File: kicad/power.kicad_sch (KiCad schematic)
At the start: 51 parts, among them J4 TYPE-C-31-M-12, Q7 BC847BW,115, U10 MC34063AD, U11 MC34063AD, U12 XC6206P332MR-G, U13 TPS2116DRLR, U9 TPD4S012DRYR

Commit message: [kicad] Fixed inductor footprints | TODO: integrate in actual pcb
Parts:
- L1, L2: footprint Inductor_SMD:L_1210_3225Metric -> bldc:CY105-100uH
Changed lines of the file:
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@@
       (effects (font (size 1.27 1.27)))
     )
-    (property "Footprint" "Inductor_SMD:L_1210_3225Metric" (at 45.72 85.09 0)
+    (property "Footprint" "bldc:CY105-100uH" (at 45.72 85.09 0)
       (effects (font (size 1.27 1.27)) hide)
     )
@@
       (effects (font (size 1.27 1.27)))
     )
-    (property "Footprint" "Inductor_SMD:L_1210_3225Metric" (at 43.18 34.29 0)
-      (effects (font (size 1.27 1.27)) hide)
-    )
+    (property "Footprint" "bldc:CY105-100uH" (at 43.18 34.29 0)
+      (effects (font (size 1.27 1.27)) hide)
+    )

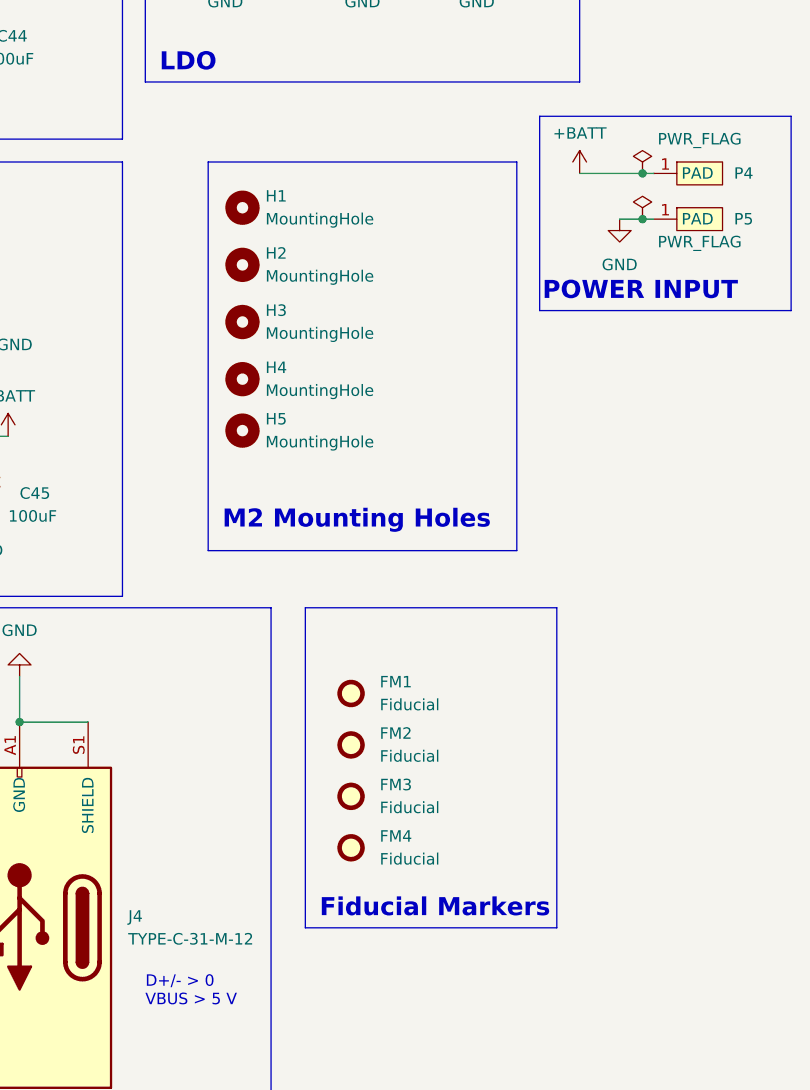
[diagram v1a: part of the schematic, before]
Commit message: changed inductors, rearranged new FET footprints and symbols
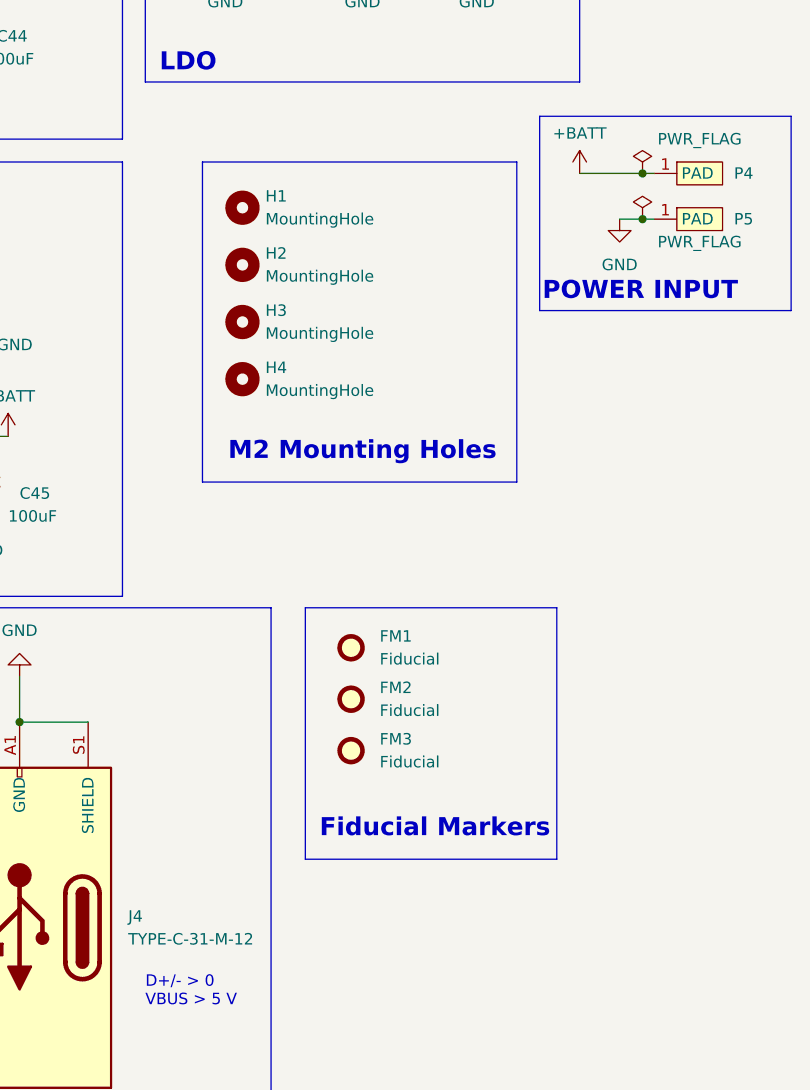
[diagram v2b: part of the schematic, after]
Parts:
- removed FM4: Fiducial, Fiducial:Fiducial_1mm_Mask2mm, symbol Mechanical:Fiducial
- removed H5: MountingHole, bldc:MountingHole_1.152mm_jlcpcb, symbol Mechanical:MountingHole
- L1, L2: footprint bldc:CY105-100uH -> L_Sunlord_SWPA6045S; MFR.Part (none) -> SWPA6045S101MT; jlcpcb (none) -> C60633
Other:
- moved on the sheet: FM1, FM2, FM3
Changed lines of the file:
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@@
     (fill (type none))
   )
-  (rectangle (start 127 114.3) (end 154.94 149.86)
+  (rectangle (start 127 114.3) (end 154.94 142.24)
     (stroke (width 0) (type default))
     (fill (type none))
@@
     (fill (type none))
   )
-  (rectangle (start 116.205 64.77) (end 150.495 107.95)
+  (rectangle (start 115.57 64.77) (end 150.495 100.33)
     (stroke (width 0) (type default))
     (fill (type none))
@@
   )
   (text_box "Fiducial Markers"
-    (at 127 144.78 0) (size 34.29 5.08)
+    (at 127 135.89 0) (size 34.29 5.08)
     (stroke (width -0.0001) (type default))
     (fill (type none))
@@
   )
   (text_box "M2 Mounting Holes"
-    (at 116.205 101.6 0) (size 34.29 5.08)
+    (at 116.84 93.98 0) (size 34.29 5.08)
     (stroke (width -0.0001) (type default))
     (fill (type none))
@@
     )
   )
-  (symbol (lib_id "Mechanical:Fiducial") (at 132.08 123.825 0) (unit 1)
-    (in_bom yes) (on_board yes) (dnp no) (fields_autoplaced)
-    (property "Reference" "FM1" (at 135.255 122.555 0)
-      (effects (font (size 1.27 1.27)) (justify left))
-    )
-    (property "Value" "Fiducial" (at 135.255 125.095 0)
-      (effects (font (size 1.27 1.27)) (justify left))
-    )
-    (property "Footprint" "Fiducial:Fiducial_1mm_Mask2mm" (at 132.08 123.825 0)
-      (effects (font (size 1.27 1.27)) hide)
-    )
-    (property "Datasheet" "~" (at 132.08 123.825 0)
+  (symbol (lib_id "Mechanical:Fiducial") (at 132.08 118.745 0) (unit 1)
+    (in_bom yes) (on_board yes) (dnp no) (fields_autoplaced)
+    (property "Reference" "FM1" (at 135.255 117.475 0)
+      (effects (font (size 1.27 1.27)) (justify left))
+    )
+    (property "Value" "Fiducial" (at 135.255 120.015 0)
+      (effects (font (size 1.27 1.27)) (justify left))
+    )
+    (property "Footprint" "Fiducial:Fiducial_1mm_Mask2mm" (at 132.08 118.745 0)
+      (effects (font (size 1.27 1.27)) hide)
+    )
+    (property "Datasheet" "~" (at 132.08 118.745 0)
       (effects (font (size 1.27 1.27)) hide)
     )
@@
       (effects (font (size 1.27 1.27)))
     )
-    (property "Footprint" "bldc:CY105-100uH" (at 45.72 85.09 0)
-      (effects (font (size 1.27 1.27)) hide)
-    )
-    (property "Datasheet" "https://wmsc.lcsc.com/wmsc/upload/file/pdf/v2/lcsc/2208231730_SHOU-HAN-CY105-100uH_C5140330.pdf" (at 45.72 85.09 0)
+    (property "Footprint" "L_Sunlord_SWPA6045S" (at 45.72 85.09 0)
+      (effects (font (size 1.27 1.27)) hide)
+    )
+    (property "Datasheet" "https://wmsc.lcsc.com/wmsc/upload/file/pdf/v2/lcsc/2310251551_Sunlord-SWPA6045S101MT_C60633.pdf" (at 45.72 85.09 0)
+      (effects (font (size 1.27 1.27)) hide)
+    )
+    (property "MFR.Part" "SWPA6045S101MT" (at 45.72 85.09 0)
+      (effects (font (size 1.27 1.27)) hide)
+    )
+    (property "jlcpcb" "C60633" (at 45.72 85.09 0)
       (effects (font (size 1.27 1.27)) hide)
     )
@@
       (effects (font (size 1.27 1.27)))
     )
-    (property "Footprint" "bldc:CY105-100uH" (at 43.18 34.29 0)
-      (effects (font (size 1.27 1.27)) hide)
-    )
-    (property "Datasheet" "https://wmsc.lcsc.com/wmsc/upload/file/pdf/v2/lcsc/2208231730_SHOU-HAN-CY105-100uH_C5140330.pdf" (at 43.18 34.29 0)
+    (property "Footprint" "L_Sunlord_SWPA6045S" (at 43.18 34.29 0)
+      (effects (font (size 1.27 1.27)) hide)
+    )
+    (property "Datasheet" "https://wmsc.lcsc.com/wmsc/upload/file/pdf/v2/lcsc/2310251551_Sunlord-SWPA6045S101MT_C60633.pdf" (at 43.18 34.29 0)
+      (effects (font (size 1.27 1.27)) hide)
+    )
+    (property "MFR.Part" "SWPA6045S101MT" (at 43.18 34.29 0)
+      (effects (font (size 1.27 1.27)) hide)
+    )
+    (property "jlcpcb" "C60633" (at 43.18 34.29 0)
       (effects (font (size 1.27 1.27)) hide)
     )
@@
     )
   )
-  (symbol (lib_id "Mechanical:MountingHole") (at 120.015 94.615 0) (unit 1)
-    (in_bom yes) (on_board yes) (dnp no) (fields_autoplaced)
-    (property "Reference" "H5" (at 122.555 93.345 0)
-      (effects (font (size 1.27 1.27)) (justify left))
-    )
-    (property "Value" "MountingHole" (at 122.555 95.885 0)
-      (effects (font (size 1.27 1.27)) (justify left))
-    )
-    (property "Footprint" "bldc:MountingHole_1.152mm_jlcpcb" (at 120.015 94.615 0)
-      (effects (font (size 1.27 1.27)) hide)
-    )
-    (property "Datasheet" "~" (at 120.015 94.615 0)
-      (effects (font (size 1.27 1.27)) hide)
-    )
-    (instances
-      (project "bldc_project"
-        (path "/91e2f46a-700b-4d7a-a06a-22469f63223f/53dc30ee-9af6-4771-8676-c78726df5d90"
-          (reference "H5") (unit 1)
-        )
-      )
-    )
-  )
   (symbol (lib_id "Mechanical:MountingHole") (at 120.015 88.9 0) (unit 1)
     (in_bom yes) (on_board yes) (dnp no) (fields_autoplaced)
@@
     )
   )
-  (symbol (lib_id "Mechanical:Fiducial") (at 132.08 135.255 0) (unit 1)
-    (in_bom yes) (on_board yes) (dnp no) (fields_autoplaced)
-    (property "Reference" "FM3" (at 135.255 133.985 0)
-      (effects (font (size 1.27 1.27)) (justify left))
-    )
-    (property "Value" "Fiducial" (at 135.255 136.525 0)
-      (effects (font (size 1.27 1.27)) (justify left))
-    )
-    (property "Footprint" "Fiducial:Fiducial_1mm_Mask2mm" (at 132.08 135.255 0)
-      (effects (font (size 1.27 1.27)) hide)
-    )
-    (property "Datasheet" "~" (at 132.08 135.255 0)
+  (symbol (lib_id "Mechanical:Fiducial") (at 132.08 130.175 0) (unit 1)
+    (in_bom yes) (on_board yes) (dnp no) (fields_autoplaced)
+    (property "Reference" "FM3" (at 135.255 128.905 0)
+      (effects (font (size 1.27 1.27)) (justify left))
+    )
+    (property "Value" "Fiducial" (at 135.255 131.445 0)
+      (effects (font (size 1.27 1.27)) (justify left))
+    )
+    (property "Footprint" "Fiducial:Fiducial_1mm_Mask2mm" (at 132.08 130.175 0)
+      (effects (font (size 1.27 1.27)) hide)
+    )
+    (property "Datasheet" "~" (at 132.08 130.175 0)
       (effects (font (size 1.27 1.27)) hide)
     )
@@
     )
   )
-  (symbol (lib_id "Mechanical:Fiducial") (at 132.08 140.97 0) (unit 1)
-    (in_bom yes) (on_board yes) (dnp no) (fields_autoplaced)
-    (property "Reference" "FM4" (at 135.255 139.7 0)
-      (effects (font (size 1.27 1.27)) (justify left))
-    )
-    (property "Value" "Fiducial" (at 135.255 142.24 0)
-      (effects (font (size 1.27 1.27)) (justify left))
-    )
-    (property "Footprint" "Fiducial:Fiducial_1mm_Mask2mm" (at 132.08 140.97 0)
-      (effects (font (size 1.27 1.27)) hide)
-    )
-    (property "Datasheet" "~" (at 132.08 140.97 0)
-      (effects (font (size 1.27 1.27)) hide)
-    )
-    (instances
-      (project "bldc_project"
-        (path "/91e2f46a-700b-4d7a-a06a-22469f63223f/53dc30ee-9af6-4771-8676-c78726df5d90"
-          (reference "FM4") (unit 1)
-        )
-      )
-    )
-  )
   (symbol (lib_id "power:+10V") (at 19.05 85.09 0) (unit 1)
     (in_bom yes) (on_board yes) (dnp no) (fields_autoplaced)
@@
     )
   )
-  (symbol (lib_id "Mechanical:Fiducial") (at 132.08 129.54 0) (unit 1)
-    (in_bom yes) (on_board yes) (dnp no) (fields_autoplaced)
-    (property "Reference" "FM2" (at 135.255 128.27 0)
-      (effects (font (size 1.27 1.27)) (justify left))
-    )
-    (property "Value" "Fiducial" (at 135.255 130.81 0)
-      (effects (font (size 1.27 1.27)) (justify left))
-    )
-    (property "Footprint" "Fiducial:Fiducial_1mm_Mask2mm" (at 132.08 129.54 0)
-      (effects (font (size 1.27 1.27)) hide)
-    )
-    (property "Datasheet" "~" (at 132.08 129.54 0)
-      (effects (font (size 1.27 1.27)) hide)
-    )
+  (symbol (lib_id "Mechanical:Fiducial") (at 132.08 124.46 0) (unit 1)
+    (in_bom yes) (on_board yes) (dnp no) (fields_autoplaced)
+    (property "Reference" "FM2" (at 135.255 123.19 0)
+      (effects (font (size 1.27 1.27)) (justify left))
+    )
+    (property "Value" "Fiducial" (at 135.255 125.73 0)
+      (effects (font (size 1.27 1.27)) (justify left))
+    )
+    (property "Footprint" "Fiducial:Fiducial_1mm_Mask2mm" (at 132.08 124.46 0)
+      (effects (font (size 1.27 1.27)) hide)
+    )
+    (property "Datasheet" "~" (at 132.08 124.46 0)
+      (effects (font (size 1.27 1.27)) hide)
+    )

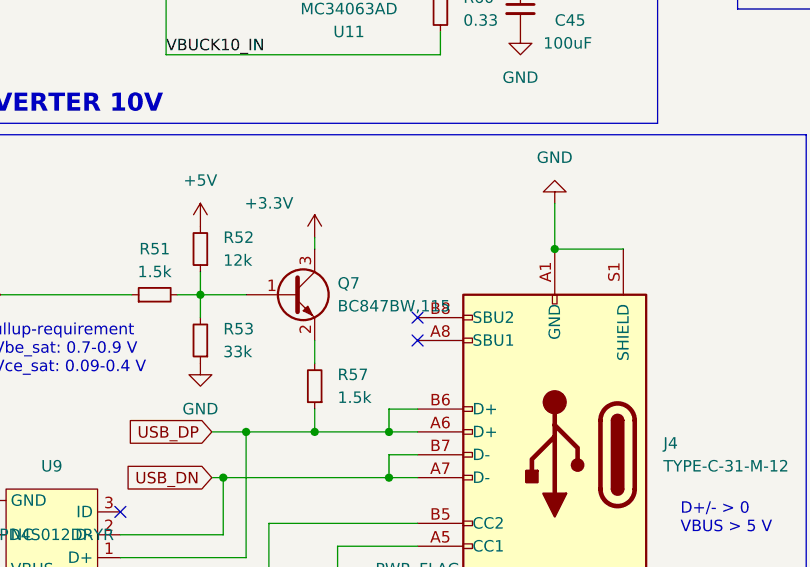
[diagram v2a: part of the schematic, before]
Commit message: [kicad] Rechecked all footprints and components requirements | TODO: think about replacing the ESD package with something else [simulations] Checked simulations of buck converter with reality
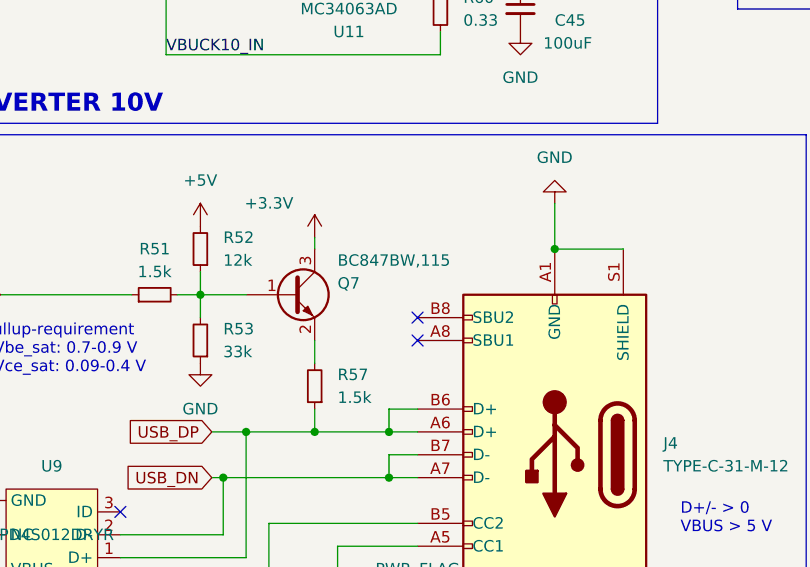
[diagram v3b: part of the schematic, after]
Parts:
- R49, R50, R53, R61, R62: MFR.Part (none) -> 0603WAF3302T5E
- R51, R54, R55, R57, R63: MFR.Part (none) -> 0805W8F1501T5E
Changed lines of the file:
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@@
+      (effects (font (size 1.27 1.27)) hide)
+    )
+    (property "MFR.Part" "0603WAF3302T5E" (at 46.99 170.18 0)
       (effects (font (size 1.27 1.27)) hide)
     )
@@
     )
     (property "jlcpcb" "C4310" (at 68.58 142.24 0)
+      (effects (font (size 1.27 1.27)) hide)
+    )
+    (property "MFR.Part" "0805W8F1501T5E" (at 68.58 142.24 0)
       (effects (font (size 1.27 1.27)) hide)
     )
@@
       (effects (font (size 1.27 1.27)) hide)
     )
+    (property "MFR.Part" "0603WAF3302T5E" (at 227.33 29.21 0)
+      (effects (font (size 1.27 1.27)) hide)
+    )
     (pin "1")
     (pin "2")
@@
   )
   (symbol (lib_id "Transistor_BJT:BC847") (at 66.04 132.08 0) (unit 1)
-    (in_bom yes) (on_board yes) (dnp no) (fields_autoplaced)
+    (in_bom yes) (on_board yes) (dnp no)
     (property "Reference" "Q7" (at 71.12 130.81 0)
       (effects (font (size 1.27 1.27)) (justify left))
     )
-    (property "Value" "BC847BW,115" (at 71.12 133.35 0)
+    (property "Value" "BC847BW,115" (at 71.12 128.27 0)
       (effects (font (size 1.27 1.27)) (justify left))
     )
@@
     )
     (property "jlcpcb" "C4310" (at 252.73 31.75 0)
+      (effects (font (size 1.27 1.27)) hide)
+    )
+    (property "MFR.Part" "0805W8F1501T5E" (at 252.73 31.75 0)
       (effects (font (size 1.27 1.27)) hide)
     )
@@
       (effects (font (size 1.27 1.27)) hide)
     )
+    (property "MFR.Part" "0805W8F1501T5E" (at 62.23 74.93 0)
+      (effects (font (size 1.27 1.27)) hide)
+    )
     (pin "1")
     (pin "2")
@@
     )
     (property "jlcpcb" "C4216" (at 46.99 182.245 0)
+      (effects (font (size 1.27 1.27)) hide)
+    )
+    (property "MFR.Part" "0603WAF3302T5E" (at 46.99 182.245 0)
       (effects (font (size 1.27 1.27)) hide)
     )
@@
       (effects (font (size 1.27 1.27)) hide)
     )
+    (property "MFR.Part" "0603WAF3302T5E" (at 55.88 137.16 0)
+      (effects (font (size 1.27 1.27)) hide)
+    )
     (pin "2")
     (pin "1")
@@
     )
     (property "jlcpcb" "C4310" (at 59.69 24.13 90)
+      (effects (font (size 1.27 1.27)) hide)
+    )
+    (property "MFR.Part" "0805W8F1501T5E" (at 59.69 24.13 0)
       (effects (font (size 1.27 1.27)) hide)
     )
@@
     )
     (property "jlcpcb" "C4216" (at 227.33 34.29 0)
+      (effects (font (size 1.27 1.27)) hide)
+    )
+    (property "MFR.Part" "0603WAF3302T5E" (at 227.33 34.29 0)
       (effects (font (size 1.27 1.27)) hide)
     )
@@
       (effects (font (size 1.27 1.27)) hide)
     )
+    (property "MFR.Part" "0805W8F1501T5E" (at 50.8 132.08 0)
+      (effects (font (size 1.27 1.27)) hide)
+    )
